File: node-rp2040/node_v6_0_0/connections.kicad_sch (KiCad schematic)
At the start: 16 parts, among them J1 Conn_01x02_Pin, J2 U.FL, J3 Conn_Coaxial, J4 Conn_02x08_Odd_Even, J5 Conn_02x02_Odd_Even, J6 U.FL, J7 Conn_01x02_Pin, J8 Conn_01x02_Pin, J9 U.FL

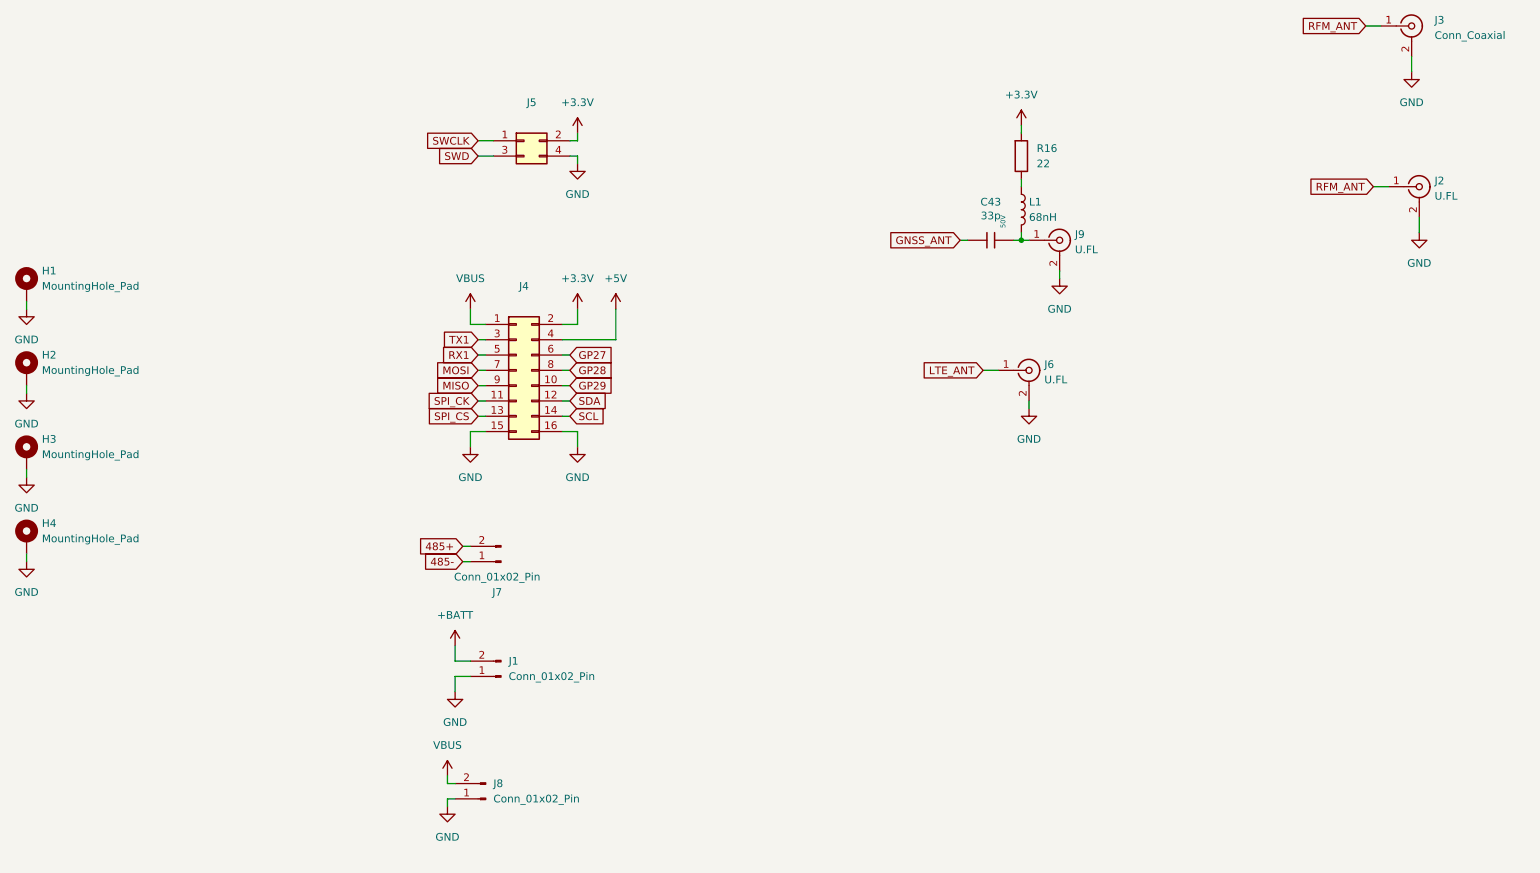
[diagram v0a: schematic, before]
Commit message: i should have made this more than one commit but: 1) started poking around in v5 to find and solve a sim card problem, forgot about it and moved on 2) created v6, modified the schematic somewhat, removed some parts, began laying out the pcb again this time as a 6 layer board 3) fixed the library setup so now it uses symbols and footprints from the packages available alongside kicad (in void linux at least) for all standard stuff PLUS the wisdom libraries and the jlcpcb prefered parts library
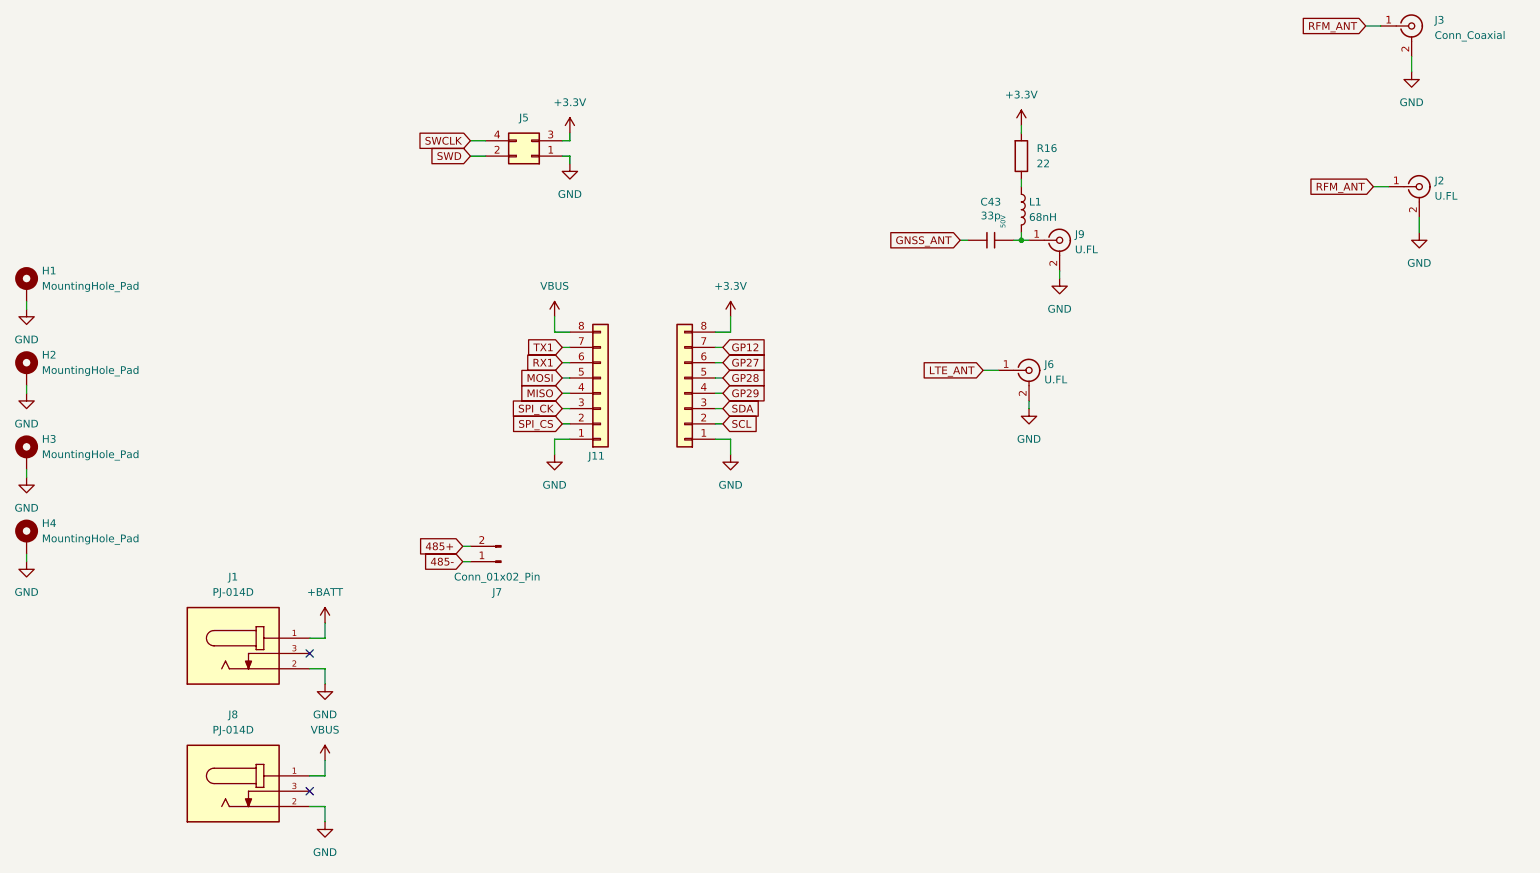
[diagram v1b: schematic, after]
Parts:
- removed J1, J8: Conn_01x02_Pin, Connector_JST:JST_PH_B2B-PH-K_1x02_P2.00mm_Vertical, symbol Connector:Conn_01x02_Pin
- removed J4: Conn_02x08_Odd_Even, Connector_PinHeader_2.54mm:PinHeader_2x08_P2.54mm_Vertical, symbol Connector_Generic:Conn_02x08_Odd_Even
- added J1, J8: PJ-014D, WiSDOM:CUI_PJ-014D, symbol WiSDOM:PJ-014D
- added J11, J12: Conn_01x08, Connector_PinHeader_2.54mm:PinHeader_1x08_P2.54mm_Vertical, symbol Connector_Generic:Conn_01x08
- C43: footprint JLCPCB-Kicad-Footprints:C_0402 -> JLCPCB:C_0402
- J2, J6, J9: footprint JLCPCB-Kicad-Footprints:IPEX-SMD_BWIPX-1-001E -> JLCPCB:IPEX-SMD_BWIPX-1-001E
- R16: footprint JLCPCB-Kicad-Footprints:R_0805 -> JLCPCB:R_0805
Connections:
- net +3.3V: now also J5.3 (Pin_3), J12.8 (Pin_8); no longer J5.2 (Pin_2)
- net +BATT: now also J1.1
- net GND: now also J5.1 (Pin_1), J1.2, J11.1 (Pin_1), J12.1 (Pin_1), J8.2; no longer J5.4 (Pin_4)
- net GP27: now also J12.6 (Pin_6)
- net GP28: now also J12.5 (Pin_5)
- net GP29: now also J12.4 (Pin_4)
- net MISO: now also J11.4 (Pin_4)
- net MOSI: now also J11.5 (Pin_5)
- net RX1: now also J11.6 (Pin_6)
- net SCL: now also J12.2 (Pin_2)
- net SDA: now also J12.3 (Pin_3)
- net SPI_CK: now also J11.3 (Pin_3)
- net SPI_CS: now also J11.2 (Pin_2)
- net SWCLK: now also J5.4 (Pin_4); no longer J5.1 (Pin_1)
- net SWD: now also J5.2 (Pin_2); no longer J5.3 (Pin_3)
- net TX1: now also J11.7 (Pin_7)
- net VBUS: now also J11.8 (Pin_8), J8.1
- new net GP12: J12.7 (Pin_7)
- no-connect marks 0 -> 2
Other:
- moved on the sheet: J5
